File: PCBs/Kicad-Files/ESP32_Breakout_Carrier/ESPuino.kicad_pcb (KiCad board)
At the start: 2 copper layers, 72.4 x 82.6 mm, 17 parts, among them J1 SD-Card Reader, J2 RFID-RC522, J3 Adafruit MAX98357, J4 Rotary Encode, J5 Next, J6 Prev, J7 Pause, J8 WS2812, J9 Power, Q1 BC337, Q2 IRF9540N, U1 ESP32-DEVKITC-32U

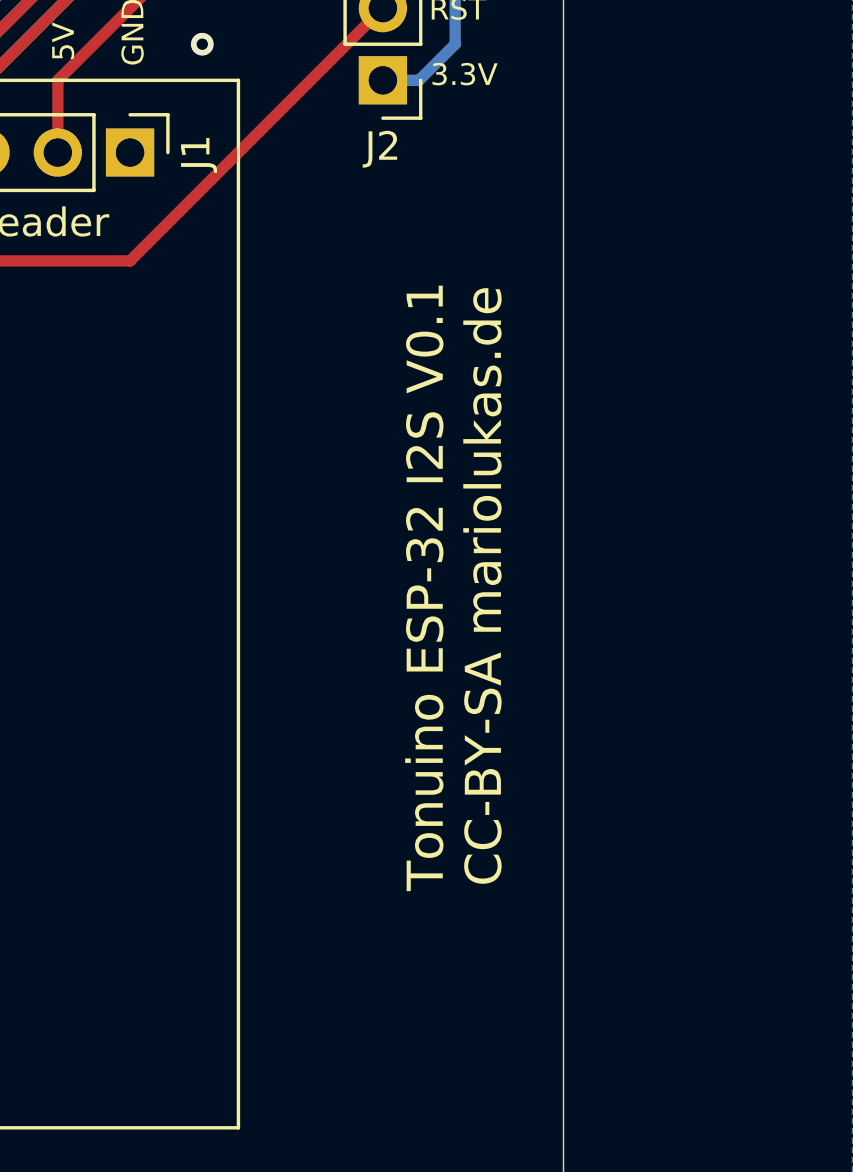
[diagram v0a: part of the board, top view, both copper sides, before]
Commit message: KiCad-Files umbenennen: ESP32_Breakout_Carrier
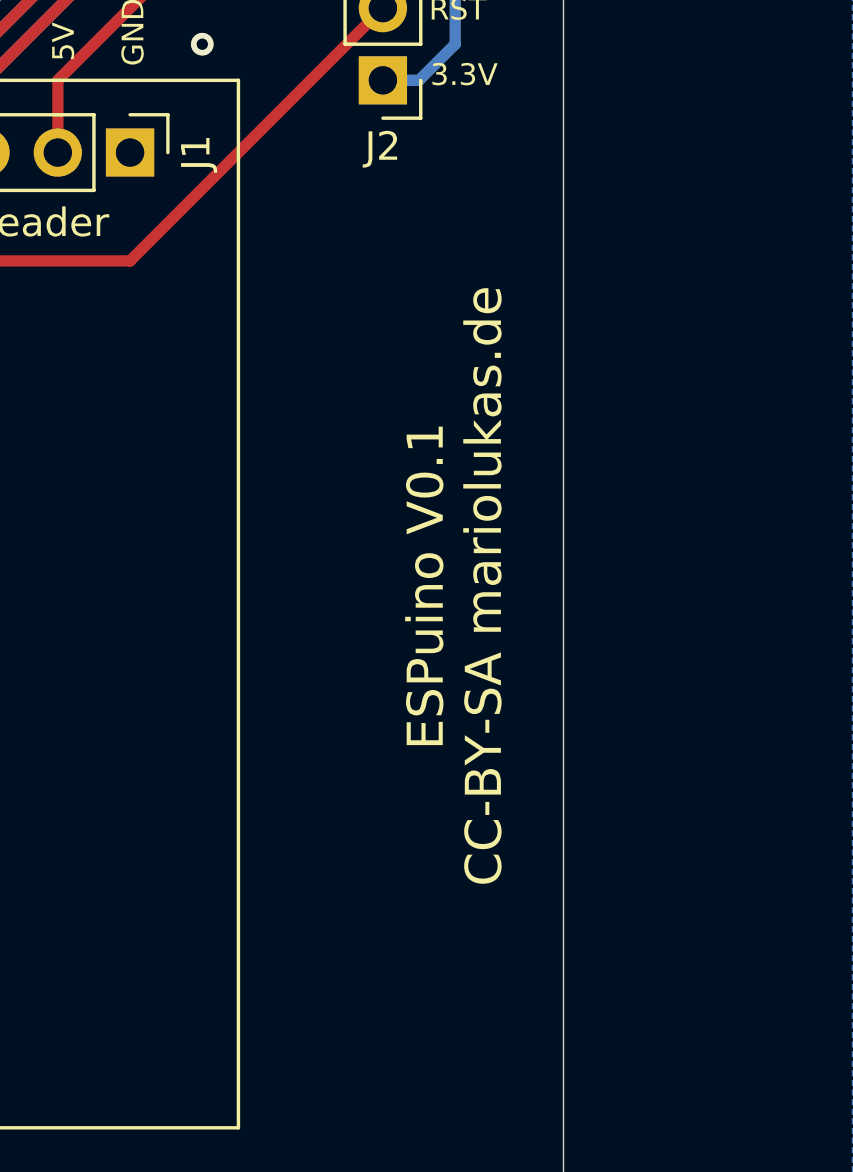
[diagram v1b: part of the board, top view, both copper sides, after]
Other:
- board text added: "ESPuino V0.1 CC-BY-SA mariolukas.de"
- board text removed: "Tonuino ESP-32 I2S V0.1 CC-BY-SA mariolukas.de"
